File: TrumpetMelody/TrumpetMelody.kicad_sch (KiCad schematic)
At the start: 20 parts, among them SW1 SW_Push, U1 STM32F411RETx, U2 TLV62565DBVR, U3 MAX98357AETE+T

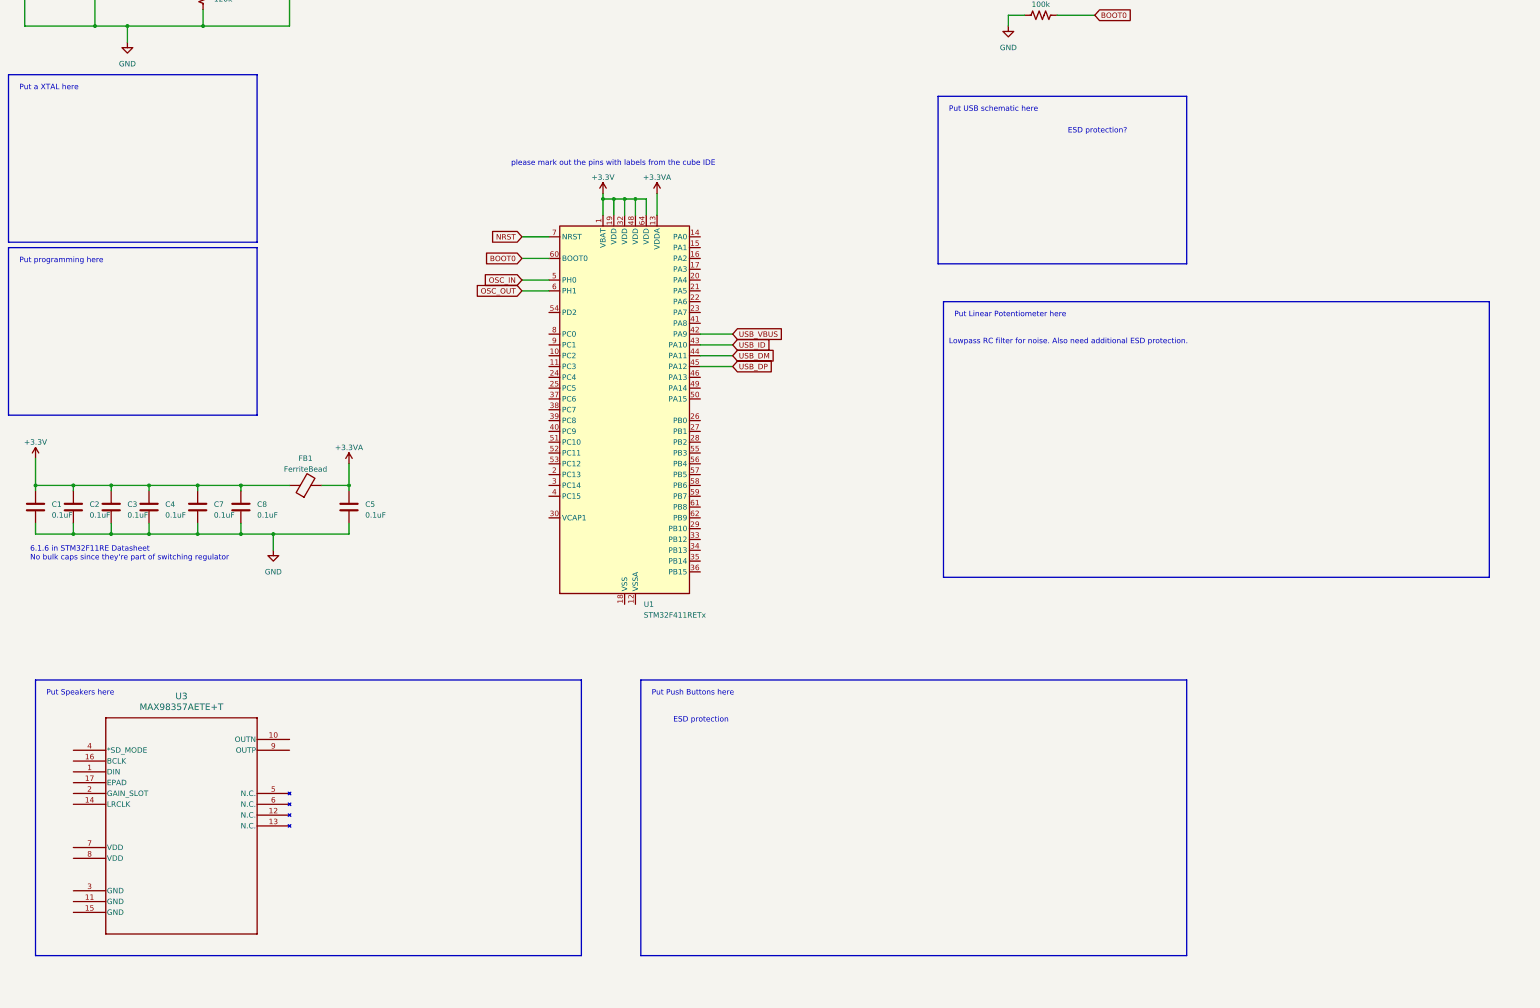
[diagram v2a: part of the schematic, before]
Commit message: Major updates, lots of first draft of components
Put in XTAL, did a bunch of research on how to select the capacitors but it comes down to actually picking an oscillator to use, we forgot to order one.
Accidentally ran into the USB micro connector schematic and that was super easy, but we might need to modify for ESD and shielding.
Tried to do the programming pins, but I had trouble finding something on how those work and how we will do it, Clayton can probably handle that another time.
Added linear potentiometer leading into 100Hz lowpass filter, and ESD
Added buttons with ESD
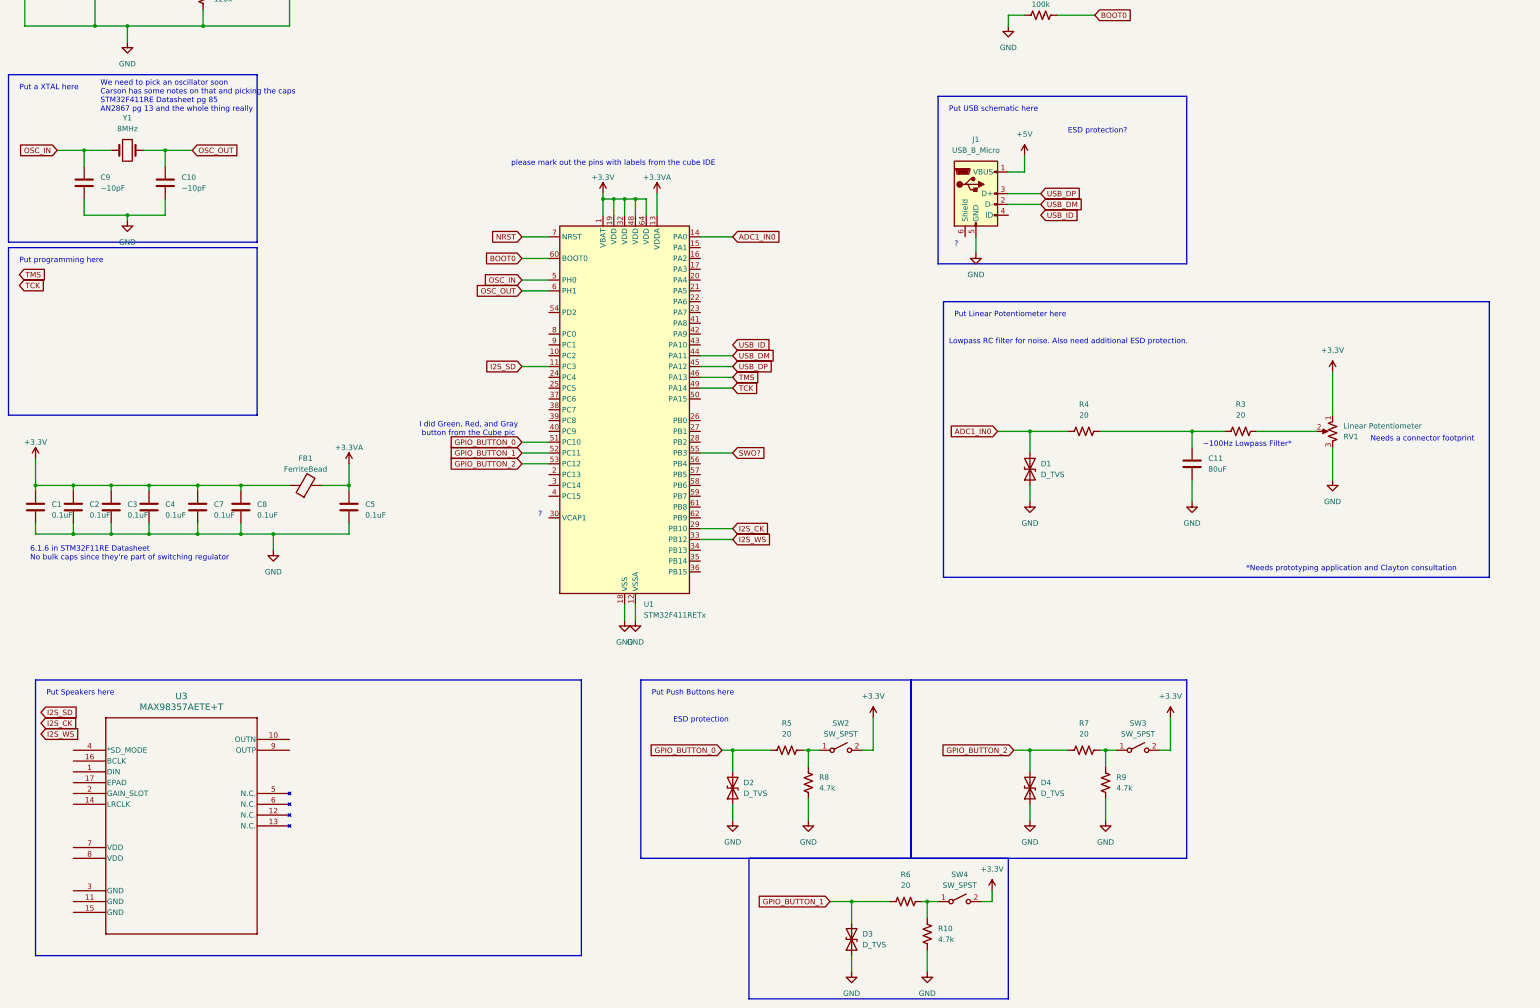
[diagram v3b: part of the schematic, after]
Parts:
- added C10, C9: ~10pF, symbol Device:C
- added C11: 80uF, symbol Device:C
- added D1, D2, D3, D4: D_TVS, symbol Device:D_TVS
- added J1: USB_B_Micro, symbol Connector:USB_B_Micro
- added R10, R8, R9: 4.7k, symbol Device:R_US
- added R3, R4, R5, R6, R7: 20, symbol Device:R_US
- added RV1: Linear Potentiometer, symbol Device:R_Potentiometer_US
- added SW2, SW3, SW4: SW_SPST, symbol Switch:SW_SPST
- added Y1: 8MHz, symbol Device:Crystal
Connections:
- net +3.3V: now also RV1.1, SW2.2 (B), SW3.2 (B), SW4.2 (B)
- net +5V: now also J1.1 (VBUS)
- net GND: now also U1.12 (VSSA), U1.18 (VSS), U1.31 (VSS), U1.47 (VSS), U1.63 (VSS), C10.2, C11.2, C9.2, D1.1 (A1), D2.1 (A1), D3.1 (A1), D4.1 (A1), J1.5 (GND), R10.1, R8.1, R9.1, RV1.3
- net OSC_IN: now also C9.1, Y1.1
- net OSC_OUT: now also C10.1, Y1.2
- net USB_DM: now also J1.2 (D-)
- net USB_DP: now also J1.3 (D+)
- net USB_ID: no longer U1.43 (PA10)
- net I2S_SD: now reaches U1.11 (PC3)
- net ADC1_IN0: now reaches U1.14 (PA0)
- net ADC1_IN0: now also D1.2 (A2), R4.1
- net I2S_CK: now reaches U1.29 (PB10)
- net I2S_WS: now reaches U1.33 (PB12)
- net TMS: now reaches U1.46 (PA13)
- net TCK: now reaches U1.49 (PA14)
- net GPIO_BUTTON_0: now reaches U1.51 (PC10)
- net GPIO_BUTTON_0: now also D2.2 (A2), R5.1
- net GPIO_BUTTON_1: now reaches U1.52 (PC11)
- net GPIO_BUTTON_1: now also D3.2 (A2), R6.1
- net GPIO_BUTTON_2: now reaches U1.53 (PC12)
- net GPIO_BUTTON_2: now also D4.2 (A2), R7.1
- net SWO?: now reaches U1.55 (PB3)
- net USB_VBUS: no longer names the net of U1.42 (PA9)
- new net: C11.1, R3.1, R4.2
- new net: R10.2, R6.2, SW4.1 (A)
- new net: R5.2, R8.2, SW2.1 (A)
- new net: R7.2, R9.2, SW3.1 (A)
- new net: R3.2, RV1.2
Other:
- note added: "*Needs prototyping application and Clayton consultation"
- note added: "?"
- note added: "I did Green, Red, and Gray button from the Cube pic"
- note added: "Needs a connector footprint"
- note added: "We need to pick an oscillator soon Carson has some notes on that and picking the caps STM32F411RE Datasheet pg 85 AN2867 pg 13 and the whole thing really"
- note added: "~100Hz Lowpass Filter*"

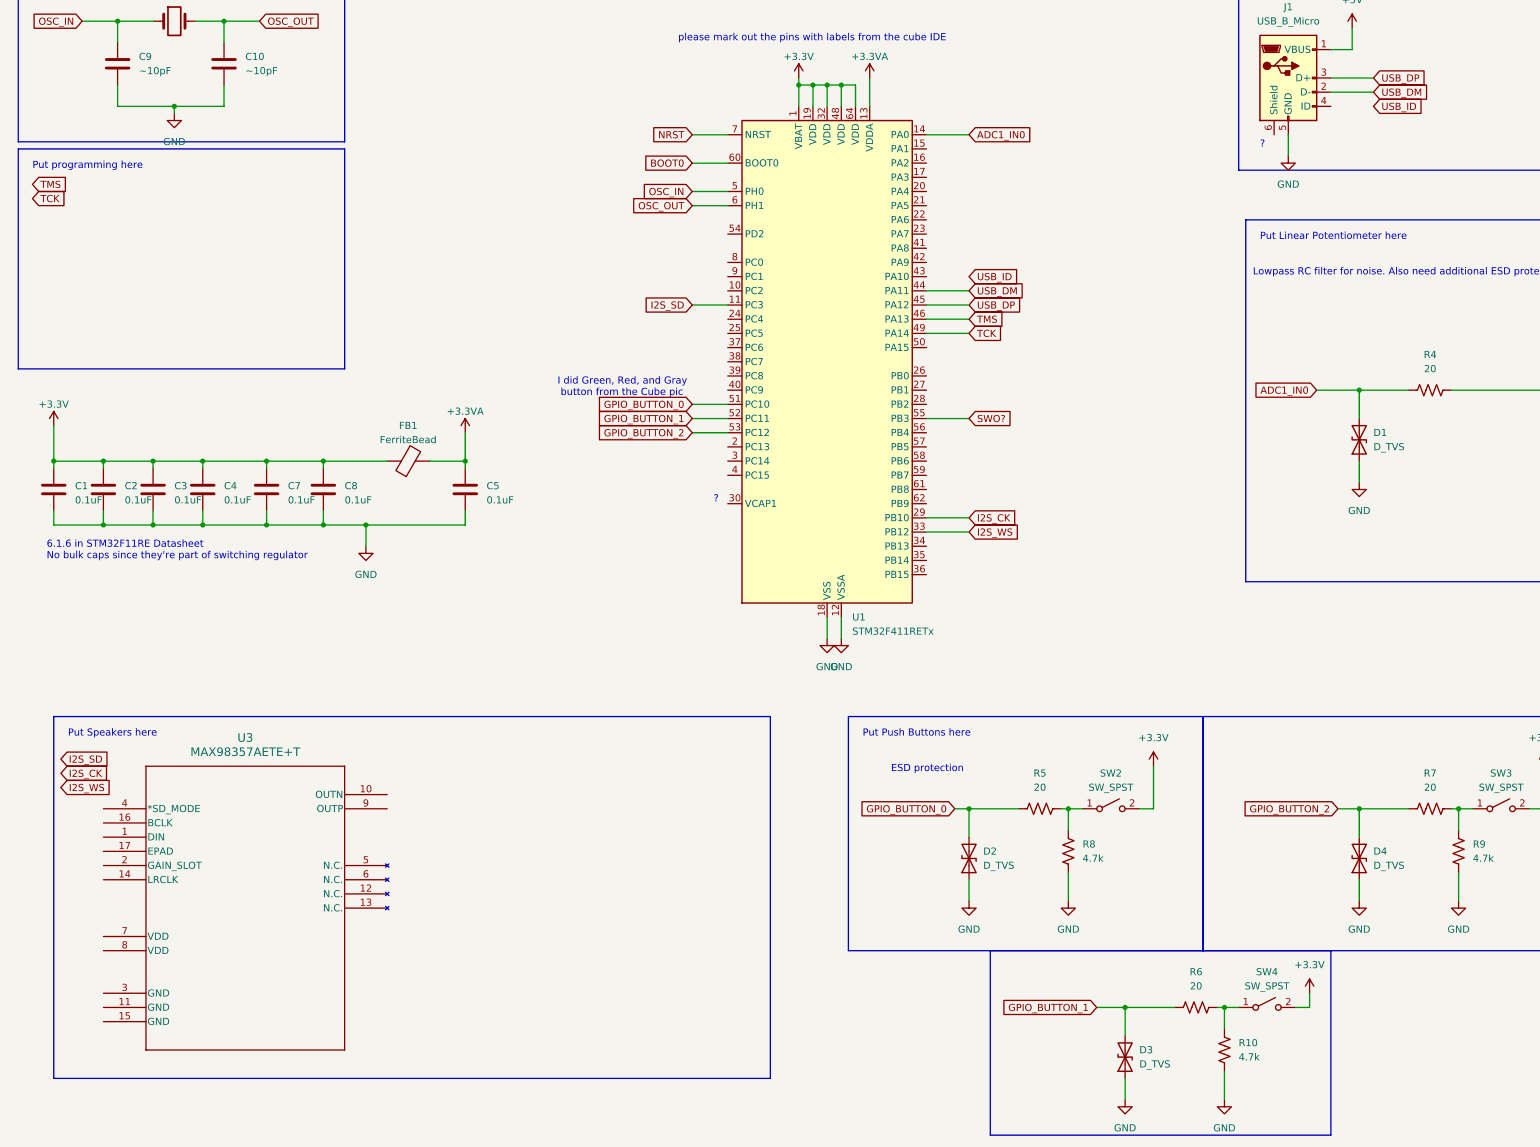
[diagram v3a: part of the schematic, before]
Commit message: Added speakers and amplifier
Yeah i think this is fine for now
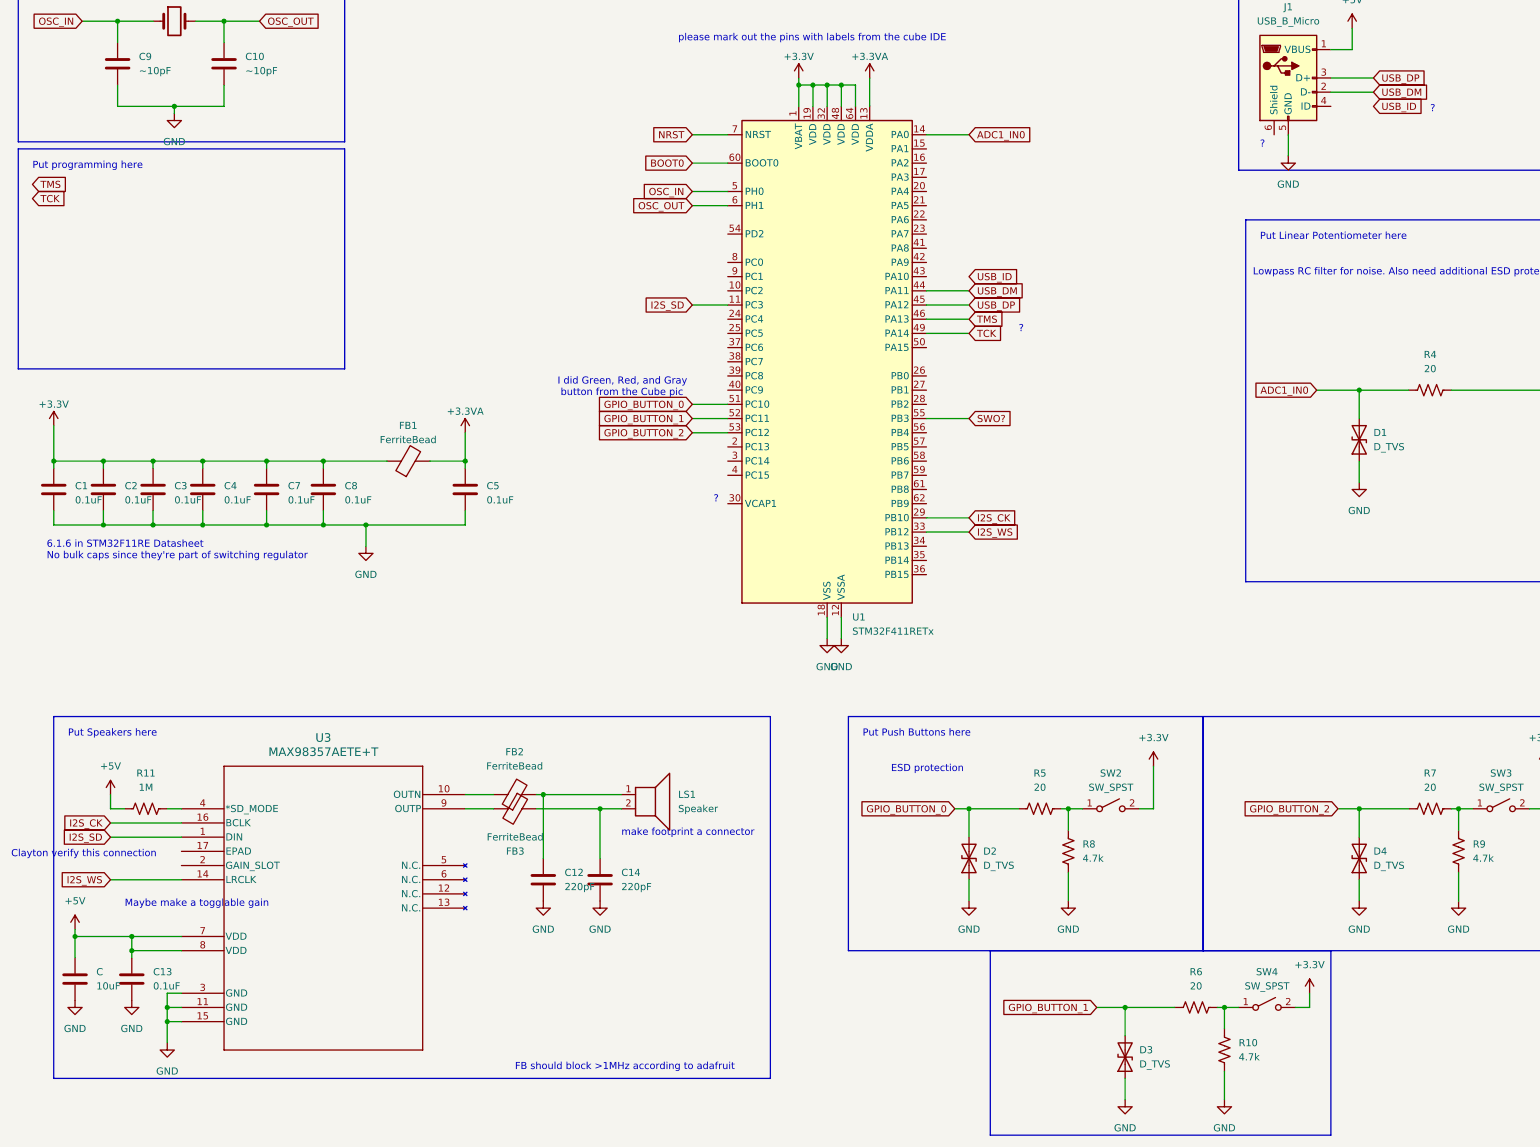
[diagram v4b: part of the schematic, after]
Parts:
- added C: 10uF, symbol Device:C
- added C12, C14: 220pF, symbol Device:C
- added C13: 0.1uF, symbol Device:C
- added FB2, FB3: FerriteBead, symbol Device:FerriteBead
- added LS1: Speaker, symbol Device:Speaker
- added R11: 1M, symbol Device:R_US
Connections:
- net +5V: now also U3.7 (VDD), U3.8 (VDD), C.1, C13.1, R11.1
- net GND: now also U3.11 (GND), U3.15 (GND), U3.3 (GND), C.2, C12.2, C13.2, C14.2
- net I2S_CK: now also U3.16 (BCLK)
- net I2S_SD: now also U3.1 (DIN)
- net I2S_WS: now also U3.14 (LRCLK)
- net at U3.10 (OUTN): now also FB2.1
- net at U3.4 (*SD_MODE): now also R11.2
- net at U3.9 (OUTP): now also FB3.2
- new net: C12.1, FB2.2, LS1.1
- new net: C14.1, FB3.1, LS1.2
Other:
- note added: "Clayton verify this connection"
- note added: "FB should block >1MHz according to adafruit"
- note added: "Maybe make a togglable gain"
- note added: "make footprint a connector"
- moved on the sheet: U3

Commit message: made manlab changes
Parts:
- added D10, D7, D8, D9: LED, symbol Device:LED
- added D5, D6: D_TVS, symbol Device:D_TVS
- added FB4: FerriteBead, symbol Device:FerriteBead
- added J2: Conn_01x05, symbol Connector_Generic:Conn_01x05
- added R12, R13: 220, symbol Device:R_US
- R10: value 4.7k -> 20
- R6: value 20 -> 4.7k
- renumbered C to C15, ERJ-6ENF5363V to ERJ-6ENF5363V1, GRM21BR60J226ME39L to GRM21BR60J226ME39L1, GRM31CR71E106KA12L to GRM31CR71E106KA12L1, LQH5BPN2R2NT0L to LQH5BPN2R2NT0L1, RC1206FR-07120KL to RC1206FR-07120KL1
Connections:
- net ADC1_IN0: now also C11.1, R3.1; no longer D1.2 (A2), R4.1
- net GND: now also R6.1, D5.1 (A1), D6.1 (A1), FB4.1; no longer C5.2, R10.1, U1.12 (VSSA)
- net GPIO_BUTTON_0: now also R8.2
- net GPIO_BUTTON_1: now also D4.2 (A2), R10.1, R9.2; no longer D3.2 (A2), R6.1
- net GPIO_BUTTON_2: now also D3.2 (A2), R6.2; no longer D4.2 (A2)
- net TCK: now also J2.2 (Pin_2)
- net TMS: now also J2.1 (Pin_1)
- net USB_DM: now also D6.2 (A2), R13.2; no longer J1.2 (D-)
- net USB_DP: now also D5.2 (A2), R12.2; no longer J1.3 (D+)
- net at R10.2, SW4.1 (A): no longer R6.2
- net at R5.2, SW2.1 (A): no longer R8.2
- net at R7.2, SW3.1 (A): no longer R9.2
- net at R3.2: now also D1.2 (A2), R4.1; no longer RV1.2
- net JTDI: now reaches U1.50 (PA15)
- net JTDI: now also J2.3 (Pin_3)
- net NJTRST: now reaches U1.56 (PB4)
- net NJTRST: now also J2.5 (Pin_5)
- net SWO? renamed SWO
- net SWO: now also J2.4 (Pin_4)
- new net: R4.2, RV1.2
- new net: J1.2 (D-), R13.1
- new net: J1.3 (D+), R12.1
- new net GNDA: C5.2, FB4.2, U1.12 (VSSA)
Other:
- note added: "Put a XTAL here Ask Joe about the one in the cabinet"
- note removed: "Clayton verify this connection"
- note removed: "Put a XTAL here"
- moved on the sheet: D1, D2, R4, R5
